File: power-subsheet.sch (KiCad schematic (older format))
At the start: 0 parts

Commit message: finished with first draft of schematic
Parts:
- added C47, C50, C52, C53, C54, C56, C57: 10uF, symbol CP_Small
- added C48: 22uF Tant, symbol CP_Small
- added C49, C51, C61: 1uF, symbol C_Small
- added C55, C59: 40mF, symbol C_Small
- added C58: 2u2F, symbol C_Small
- added C60: 0u1F, symbol C_Small
- added C62: 47pF, symbol C_Small
- added C63: 2n2F, symbol C_Small
- added C64: 10uF, symbol C_Small
- added CON1: BARREL_JACK, symbol BARREL_JACK
- added D1: D_Schottky_Small, symbol D_Schottky_Small
- added L1: 10uH, symbol L_Small
- added L2: 22uH, symbol L_Small
- added Q1, Q2, Q3, Q4: Q_NMOS_DGS, symbol Q_NMOS_DGS
- added R23: 700R, symbol R
- added R24, R26: 100R, symbol R
- added R25: 630R, symbol R
- added R27: 45k3, symbol R
- added R28: 147k, symbol R
- added R29: 10k, symbol R
- added U11: LT1085, symbol LT1085
- added U12, U14, U16: NCP1117ST50T3G_MountingTab, TO_SOT_Packages_SMD:SOT-223, symbol NCP1117ST50T3G_MountingTab
- added U13: MAX1721, symbol MAX1721
- added U15, U17: MAX6820, symbol MAX6820
- added U18: LT3580, symbol LT3580
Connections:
- net +12VA: now also Q3.3 (S)
- net +5VA: now also C52.1, R23.1, U12.2 (VO), U12.4 (VO), U13.2 (IN), U15.1 (VCC1)
- net +5VD: now also Q1.3 (S)
- net -12VA: now also Q4.3 (S)
- net GNDREF: now also C47.2, C48.2, C50.2, C51.1, C52.2, C53.2, C54.2, C55.1, C56.2, C57.2, C58.2, C59.1, C60.1, C62.2, C63.2, C64.2, CON1.2, CON1.3, D1.1 (K), R24.2, R26.2, R27.1, U11.1 (GND), U12.1 (GND), U13.4 (GND), U14.1 (GND), U15.2 (GND), U16.1 (GND), U17.2 (GND), U18.8 (SYNC), U18.9 (GND)
- new net: C48.1, C50.1, C53.1, C56.1, C58.1, L1.1, Q3.1 (D), U11.2 (VOUT), U12.3 (VI), U14.3 (VI), U16.3 (VI), U17.6 (VCC2), U18.3 (VIN), U18.5 (~SHDN)
- new net: C54.1, Q1.1 (D), U14.2 (VO), U14.4 (VO)
- new net: C57.1, Q2.1 (D), U15.6 (VCC2), U16.2 (VO), U16.4 (VO)
- new net: C47.1, CON1.1, U11.3 (VIN)
- new net: R25.2, R26.1, U17.3 (SETV)
- new net: C59.2, U17.4 (SETD)
- new net: Q3.2 (G), Q4.2 (G), U17.5 (GATE)
- new net: R23.2, R24.1, U15.3 (SETV)
- new net: C55.2, U15.4 (SETD)
- new net: Q1.2 (G), Q2.2 (G), U15.5 (GATE)
- new net: C49.1, U13.3 (C1-)
- new net: C49.2, U13.6 (C1+)
- new net: C64.1, L2.2, Q4.1 (D), R28.2
- new net: R28.1, U18.1 (FB)
- new net: C62.1, R29.1, U18.2 (VC)
- new net: C61.1, L1.2, U18.4 (SW)
- new net: R27.2, U18.6 (RT)
- new net: C60.2, U18.7 (SS)
- new net: C61.2, D1.2 (A), L2.1
- new net: C63.1, R29.2
- new net +5VP: Q2.3 (S), R25.1, U17.1 (VCC1)
- new net -5V: C51.2, U13.1 (OUT)
- no-connect marks 0 -> 1
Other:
- note added: "+12V -> -12V conversion"
- note added: "+5V -> -5V conversion"
- note added: "12V DC output regulator"
- note added: "2u2F cap = 25V X5R, 1206\n10uF cap = 25V X5R, 1206\n1uF cap = 50V X5R, 0805\nDiode = Central Semi CMMSH1-40\n10uH = SUMIDA CDRH6D28NP-100NC\n22uH = SUMIDA CDRH6D28NP-220NC"
- note added: "Power sequence:\n1) +5VA, -5V\n2) +5VP, +5VD\n3) +12VA, -12VA"
- note added: "Rtop = Rbottom ((VTRIP / 0.618) - 1) \n"
- note added: "tDELAY (s) = 2.48 s/Farad * CSET (F)\n!Verify before production!"

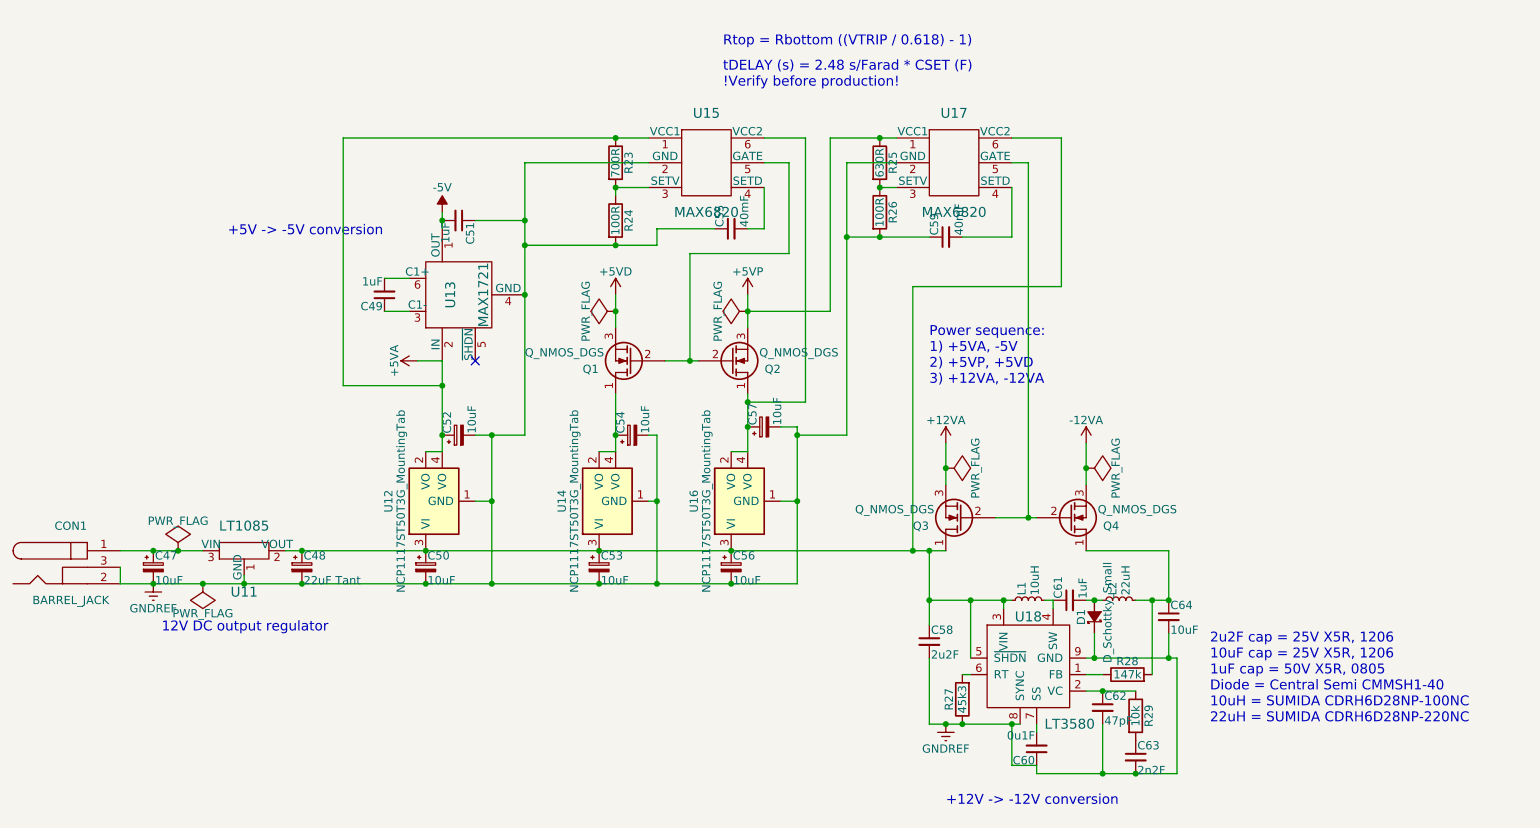
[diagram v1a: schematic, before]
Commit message: finalized schematic, finishing footprint assignment, starting pcb layout
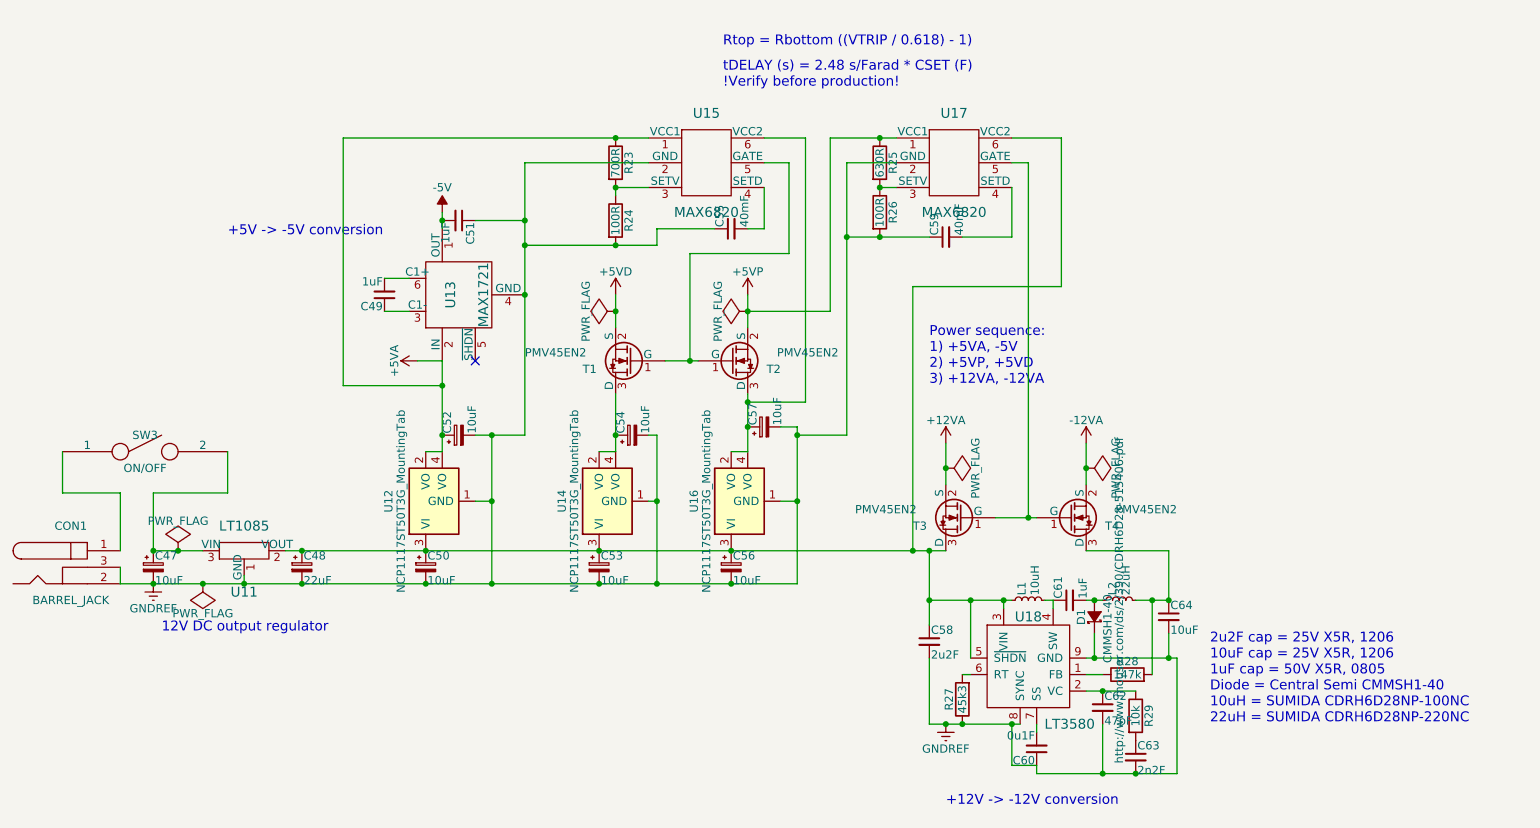
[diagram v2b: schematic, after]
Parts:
- removed Q1, Q2, Q3, Q4: Q_NMOS_DGS, symbol Q_NMOS_DGS
- added SW3: ON/OFF, SW-Eswitch:M7, symbol SPST
- added T1, T2, T3, T4: PMV45EN2, TO_SOT_Packages_SMD:SOT-23, symbol PMV45EN2
- C47, C50, C52, C53, C54, C56, C57: footprint (none) -> Capacitors_Tantalum_SMD:TantalC_SizeR_EIA-2012
- C48: value 22uF Tant -> 22uF; footprint (none) -> Capacitors_Tantalum_SMD:TantalC_SizeB_EIA-3528_HandSoldering
- C49, C51, C55, C59, C60: footprint (none) -> Capacitors_SMD:C_0603_HandSoldering
- C58, C64: footprint (none) -> Capacitors_SMD:C_1206_HandSoldering
- C61, C62, C63: footprint (none) -> Capacitors_SMD:C_0805_HandSoldering
- CON1: footprint (none) -> SW-Switchcraft:L712RAS
- D1: value D_Schottky_Small -> CMMSH1-40; footprint (none) -> Diodes_SMD:SOD-123; Manufacturer (none) -> Central Semiconductor; Package ID (none) -> SOD-123F; Pricing (none) -> 0.00@0
- L1: footprint (none) -> SW-Sumida:CDRH6D28; Manufacturer (none) -> Sumida; Pricing (none) -> 0.00@0
- L2: footprint (none) -> SW-Sumida:CDRH3D28NP; Manufacturer (none) -> Sumida; Pricing (none) -> 0.00@0
- R23, R24, R25, R26: footprint (none) -> Resistors_SMD:R_0603_HandSoldering
- R27, R28, R29: footprint (none) -> Resistors_SMD:R_0805_HandSoldering
- U11: footprint (none) -> TO_SOT_Packages_THT:TO-220_Neutral123_Horizontal_LargePads
- U13, U15, U17: footprint (none) -> TO_SOT_Packages_SMD:SOT-23-6_Handsoldering
- U18: footprint (none) -> Housings_SSOP:MSOP-8-1EP_3x3mm_Pitch0.65mm
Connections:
- net +12VA: now also T3.2 (S)
- net +5VD: now also T1.2 (S)
- net +5VP: now also T2.2 (S)
- net -12VA: now also T4.2 (S)
- net at C48.1, C50.1, C53.1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: now also T3.3 (D)
- net at C54.1, U14.2 (VO), U14.4 (VO): now also T1.3 (D)
- net at C57.1, U15.6 (VCC2), U16.2 (VO)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: now also T2.3 (D)
- net at C47.1, U11.3 (VIN): now also SW3.2; no longer CON1.1
- net at U17.5 (GATE): now also T3.1 (G), T4.1 (G)
- net at U15.5 (GATE): now also T1.1 (G), T2.1 (G)
- net at C64.1, L2.2, R28.2: now also T4.3 (D)
- new net: CON1.1, SW3.1

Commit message: before initial DRC
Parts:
- C55, C59: value 40mF -> 0u01F
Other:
- note added: "tDELAY (s) = 2.48 s/Farad * (10^6) * CSET (F)\nuF as CSET will get seconds\n!Verify before production!"
- note removed: "tDELAY (s) = 2.48 s/Farad * CSET (F)\n!Verify before production!"
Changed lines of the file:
@@
 $EndDescr
 $Comp
-L +12VA #PWR092
+L +12VA #PWR093
 U 1 1 580C6FB9
 P 7100 3150
-F 0 "#PWR092" H 7100 3000 50  0001 C CNN
+F 0 "#PWR093" H 7100 3000 50  0001 C CNN
 F 1 "+12VA" H 7100 3290 50  0000 C CNN
 F 2 "" H 7100 3150 50  0000 C CNN
@@
 $EndComp
 $Comp
-L -12VA #PWR093
+L -12VA #PWR094
 U 1 1 580C6FCD
 P 7950 3150
-F 0 "#PWR093" H 7950 3000 50  0001 C CNN
+F 0 "#PWR094" H 7950 3000 50  0001 C CNN
 F 1 "-12VA" H 7950 3290 50  0000 C CNN
 F 2 "" H 7950 3150 50  0000 C CNN
@@
 $EndComp
 $Comp
-L +5VD #PWR094
+L +5VD #PWR095
 U 1 1 580C6FE1
 P 5100 2250
-F 0 "#PWR094" H 5100 2100 50  0001 C CNN
+F 0 "#PWR095" H 5100 2100 50  0001 C CNN
 F 1 "+5VD" H 5100 2390 50  0000 C CNN
 F 2 "" H 5100 2250 50  0000 C CNN
@@
 $EndComp
 $Comp
-L +5VA #PWR095
+L +5VA #PWR096
 U 1 1 580C6FF5
 P 3900 2650
-F 0 "#PWR095" H 3900 2500 50  0001 C CNN
+F 0 "#PWR096" H 3900 2500 50  0001 C CNN
 F 1 "+5VA" H 3900 2790 50  0000 C CNN
 F 2 "" H 3900 2650 50  0000 C CNN
@@
 $EndComp
 $Comp
-L GNDREF #PWR096
+L GNDREF #PWR097
 U 1 1 580C7009
 P 2300 4000
-F 0 "#PWR096" H 2300 3750 50  0001 C CNN
+F 0 "#PWR097" H 2300 3750 50  0001 C CNN
 F 1 "GNDREF" H 2300 3850 50  0000 C CNN
 F 2 "" H 2300 4000 50  0000 C CNN
@@
 $EndComp
 $Comp
-L +5VP #PWR097
+L +5VP #PWR098
 U 1 1 580B2C17
 P 5900 2250
-F 0 "#PWR097" H 5900 2100 50  0001 C CNN
+F 0 "#PWR098" H 5900 2100 50  0001 C CNN
 F 1 "+5VP" H 5900 2390 50  0000 C CNN
 F 2 "" H 5900 2250 50  0000 C CNN
@@
 $EndComp
 $Comp
-L -5V #PWR3
+L -5V #PWR103
 U 1 1 580B2D1F
 P 4050 1750
-F 0 "#PWR3" H 4050 1850 50  0001 C CNN
+F 0 "#PWR103" H 4050 1850 50  0001 C CNN
 F 1 "-5V" H 4050 1900 50  0000 C CNN
 F 2 "" H 4050 1750 50  0000 C CNN
@@
 U 1 1 580B3CA2
 P 7150 1450
-F 0 "U17" H 7150 1750 60  0000 C CNN
-F 1 "MAX6820" H 7150 1150 60  0000 C CNN
+F 0 "U17" H 7150 1500 60  0000 C CNN
+F 1 "MAX6820" H 7150 1750 60  0000 C CNN
 F 2 "TO_SOT_Packages_SMD:SOT-23-6_Handsoldering" H 6900 1400 60  0001 C CNN
 F 3 "https://datasheets.maximintegrated.com/en/ds/MAX6819-MAX6820.pdf" H 7250 850 60  0001 C CNN
@@
 U 1 1 580B3D03
 P 5650 1450
-F 0 "U15" H 5650 1750 60  0000 C CNN
-F 1 "MAX6820" H 5650 1150 60  0000 C CNN
+F 0 "U15" H 5650 1500 60  0000 C CNN
+F 1 "MAX6820" H 5650 1750 60  0000 C CNN
 F 2 "TO_SOT_Packages_SMD:SOT-23-6_Handsoldering" H 5400 1400 60  0001 C CNN
 F 3 "https://datasheets.maximintegrated.com/en/ds/MAX6819-MAX6820.pdf" H 5750 850 60  0001 C CNN
@@
 $EndComp
 $Comp
-L GNDREF #PWR098
+L GNDREF #PWR099
 U 1 1 580B63E1
 P 7100 4850
-F 0 "#PWR098" H 7100 4600 50  0001 C CNN
+F 0 "#PWR099" H 7100 4600 50  0001 C CNN
 F 1 "GNDREF" H 7100 4700 50  0000 C CNN
 F 2 "" H 7100 4850 50  0000 C CNN
@@
 U 1 1 580B9EE1
 P 5800 1850
-F 0 "C55" H 5810 1920 50  0000 L CNN
-F 1 "40mF" H 5810 1770 50  0000 L CNN
+F 0 "C55" V 5700 1850 50  0000 L CNN
+F 1 "0u01F" V 5900 1850 50  0000 L CNN
 F 2 "Capacitors_SMD:C_0603_HandSoldering" H 5800 1850 50  0001 C CNN
 F 3 "" H 5800 1850 50  0000 C CNN
@@
 $EndComp
 Text Notes 5750 1000 0    60   ~ 0
-tDELAY (s) = 2.48 s/Farad * CSET (F)\n!Verify before production!
-Text Notes 5750 750  0    60   ~ 0
+tDELAY (s) = 2.48 s/Farad * (10^6) * CSET (F)\nuF as CSET will get seconds\n!Verify before production!
+Text Notes 5750 650  0    60   ~ 0
 Rtop = Rbottom ((VTRIP / 0.618) - 1) \n
 Wire Wire Line
@@
 P 7100 1900
 F 0 "C59" H 7110 1970 50  0000 L CNN
-F 1 "40mF" H 7110 1820 50  0000 L CNN
+F 1 "0u01F" H 7110 1820 50  0000 L CNN
 F 2 "Capacitors_SMD:C_0603_HandSoldering" H 7100 1900 50  0001 C CNN
 F 3 "" H 7100 1900 50  0000 C CNN
@@
 Connection ~ 6900 3800
 $Comp
-L PWR_FLAG #FLG099
+L PWR_FLAG #FLG0100
 U 1 1 580C134B
 P 7100 3300
-F 0 "#FLG099" H 7100 3395 50  0001 C CNN
+F 0 "#FLG0100" H 7100 3395 50  0001 C CNN
 F 1 "PWR_FLAG" H 7100 3480 50  0000 C CNN
 F 2 "" H 7100 3300 50  0000 C CNN
@@
 $EndComp
 $Comp
-L PWR_FLAG #FLG0100
+L PWR_FLAG #FLG0101
 U 1 1 580C1455
 P 7950 3300
-F 0 "#FLG0100" H 7950 3395 50  0001 C CNN
+F 0 "#FLG0101" H 7950 3395 50  0001 C CNN
 F 1 "PWR_FLAG" H 7950 3480 50  0000 C CNN
 F 2 "" H 7950 3300 50  0000 C CNN
@@
 Connection ~ 4050 1800
 $Comp
-L PWR_FLAG #FLG0101
+L PWR_FLAG #FLG0102
 U 1 1 580C1C36
 P 5900 2350
-F 0 "#FLG0101" H 5900 2445 50  0001 C CNN
+F 0 "#FLG0102" H 5900 2445 50  0001 C CNN
 F 1 "PWR_FLAG" H 5900 2530 50  0000 C CNN
 F 2 "" H 5900 2350 50  0000 C CNN
@@
 $EndComp
 $Comp
-L PWR_FLAG #FLG0102
+L PWR_FLAG #FLG0103
 U 1 1 580C1CC5
 P 5100 2350
-F 0 "#FLG0102" H 5100 2445 50  0001 C CNN
+F 0 "#FLG0103" H 5100 2445 50  0001 C CNN
 F 1 "PWR_FLAG" H 5100 2530 50  0000 C CNN
 F 2 "" H 5100 2350 50  0000 C CNN
@@
 NoConn ~ 4250 2650
 $Comp
-L PWR_FLAG #FLG0103
+L PWR_FLAG #FLG0104
 U 1 1 580C30D2
 P 2450 3800
-F 0 "#FLG0103" H 2450 3895 50  0001 C CNN
+F 0 "#FLG0104" H 2450 3895 50  0001 C CNN
 F 1 "PWR_FLAG" H 2450 3980 50  0000 C CNN
 F 2 "" H 2450 3800 50  0000 C CNN
@@
 Connection ~ 2450 3800
 $Comp
-L PWR_FLAG #FLG0104
+L PWR_FLAG #FLG0105
 U 1 1 580C4729
 P 2600 4000
-F 0 "#FLG0104" H 2600 4095 50  0001 C CNN
+F 0 "#FLG0105" H 2600 4095 50  0001 C CNN
 F 1 "PWR_FLAG" H 2600 4180 50  0000 C CNN
 F 2 "" H 2600 4000 50  0000 C CNN
